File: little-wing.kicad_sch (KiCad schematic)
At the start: 126 parts, among them IC1 AP7335-WG-7, J1 nice!view, J2 Battery, J3 trackball, J4 rotary, J5 trackball, J6 nice!view, J7 Battery, SW1 Power, SW2 Reset, SW3 Reset, SW4 Power, U1 nice!nano v2, U2 PMW3610, U3 nice!nano v2

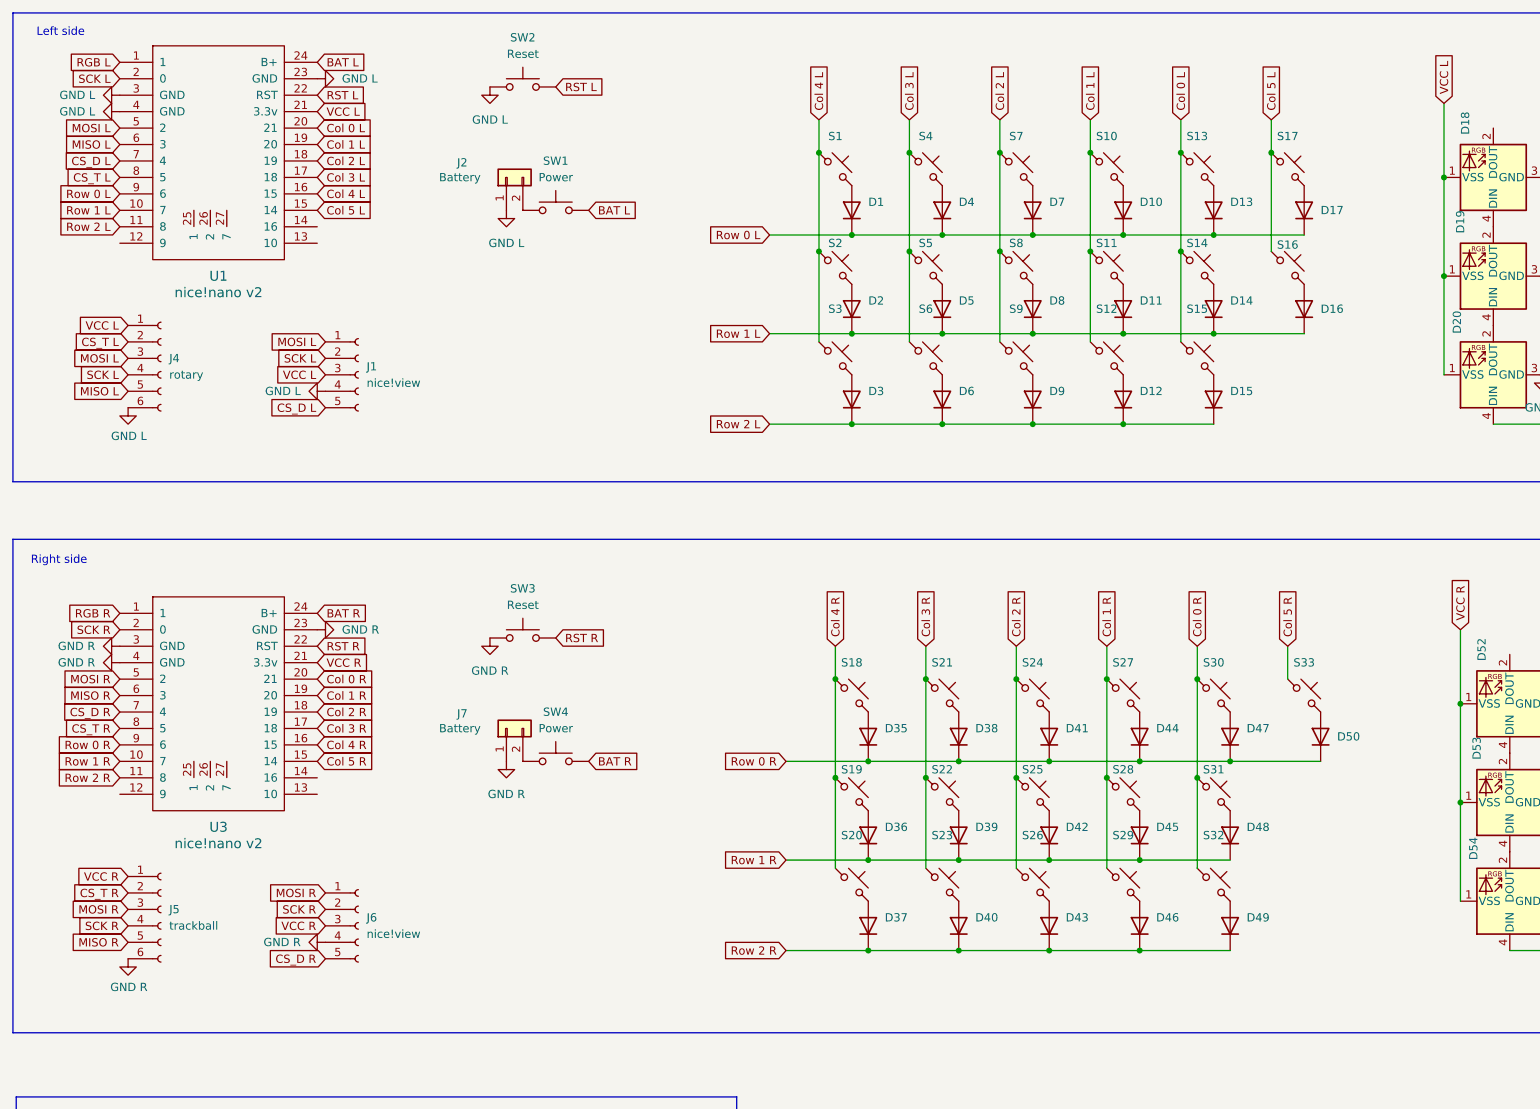
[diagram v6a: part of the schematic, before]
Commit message: Lining up some extra sockets for wiring
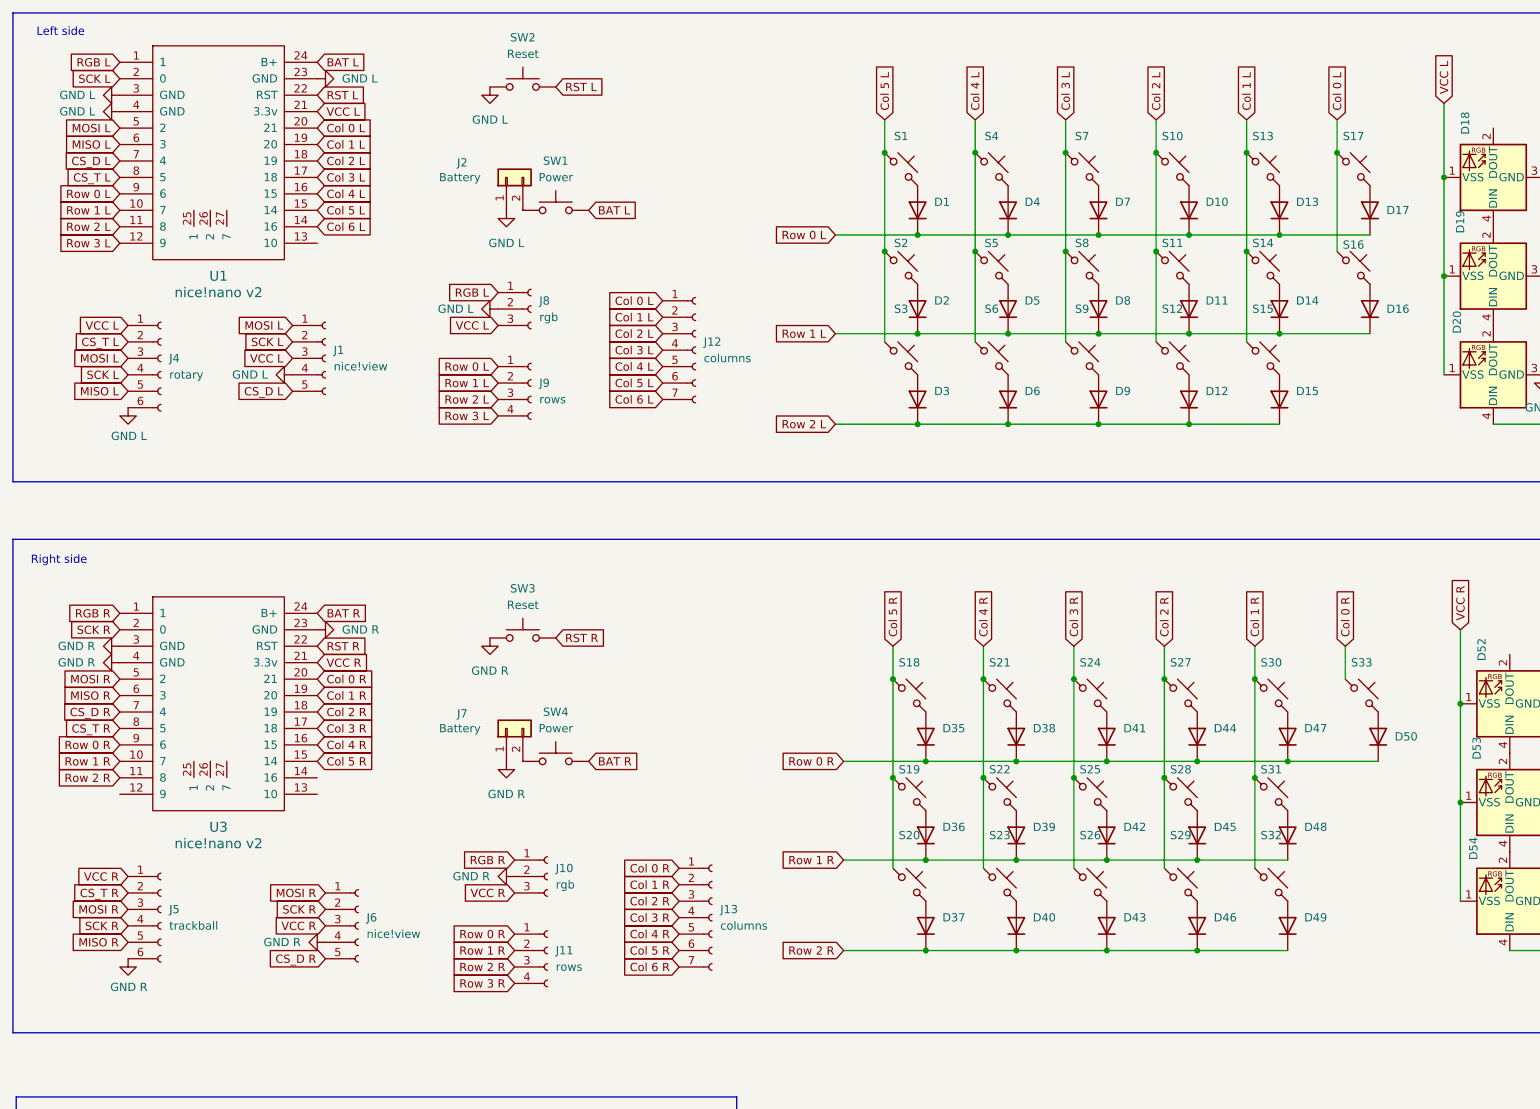
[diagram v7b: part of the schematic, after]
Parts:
- added J10, J8: rgb, Connector_Wuerth:Wuerth_WR-WTB_64800311622_1x03_P1.50mm_Vertical, symbol Connector:Conn_01x03_Socket
- added J11, J9: rows, Connector_Wuerth:Wuerth_WR-WTB_64800411622_1x04_P1.50mm_Vertical, symbol Connector:Conn_01x04_Socket
- added J12, J13: columns, Connector_Wuerth:Wuerth_WR-WTB_64800711622_1x07_P1.50mm_Vertical, symbol Connector:Conn_01x07_Socket
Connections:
- net Col 0 L: now also S16.1, S17.1, J12.1 (Pin_1); no longer S13.1, S14.1, S15.1
- net Col 0 R: now also S33.1, J13.1 (Pin_1); no longer S30.1, S31.1, S32.1
- net Col 1 L: now also S13.1, S14.1, S15.1, J12.2 (Pin_2); no longer S10.1, S11.1, S12.1
- net Col 1 R: now also S30.1, S31.1, S32.1, J13.2 (Pin_2); no longer S27.1, S28.1, S29.1
- net Col 2 L: now also S10.1, S11.1, S12.1, J12.3 (Pin_3); no longer S7.1, S8.1, S9.1
- net Col 2 R: now also S27.1, S28.1, S29.1, J13.3 (Pin_3); no longer S24.1, S25.1, S26.1
- net Col 3 L: now also S7.1, S8.1, S9.1, J12.4 (Pin_4); no longer S4.1, S5.1, S6.1
- net Col 3 R: now also S24.1, S25.1, S26.1, J13.4 (Pin_4); no longer S21.1, S22.1, S23.1
- net Col 4 L: now also S4.1, S5.1, S6.1, J12.5 (Pin_5); no longer S1.1, S2.1, S3.1
- net Col 4 R: now also S21.1, S22.1, S23.1, J13.5 (Pin_5); no longer S18.1, S19.1, S20.1
- net Col 5 L: now also S1.1, S2.1, S3.1, J12.6 (Pin_6); no longer S16.1, S17.1
- net Col 5 R: now also S18.1, S19.1, S20.1, J13.6 (Pin_6); no longer S33.1
- net GND L: now also J8.2 (Pin_2)
- net GND R: now also J10.2 (Pin_2)
- net RGB L: now also J8.1 (Pin_1)
- net RGB R: now also J10.1 (Pin_1)
- net Row 0 L: now also J9.1 (Pin_1)
- net Row 0 R: now also J11.1 (Pin_1)
- net Row 1 L: now also J9.2 (Pin_2)
- net Row 1 R: now also J11.2 (Pin_2)
- net Row 2 L: now also J9.3 (Pin_3)
- net Row 2 R: now also J11.3 (Pin_3)
- net VCC L: now also J8.3 (Pin_3)
- net VCC R: now also J10.3 (Pin_3)
- net Row 3 L: now reaches U1.12 (9)
- net Row 3 L: now also J9.4 (Pin_4)
- net Col 6 L: now reaches U1.14 (16)
- net Col 6 L: now also J12.7 (Pin_7)
- new net Col 6 R: J13.7 (Pin_7)
- new net Row 3 R: J11.4 (Pin_4)
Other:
- moved on the sheet: D1, D10, D11, D12, D13, D14, D15, D16, D17, D2, D3, D35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

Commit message: Wiring together the mobos
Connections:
- net CS_T  L is gone; now on net CS_T L: J4.2 (Pin_2)
- net SCK  L is gone; now on net SCK L: J4.4 (Pin_4)
- net Col 6 R: now also U3.14 (16)
- net Row 3 R: now also U3.12 (9)
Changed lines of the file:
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@@
 		)
 	)
-	(global_label "CS_T  L"
+	(global_label "CS_T L"
 		(shape input)
 		(at 36.83 67.31 180)
@@
 		)
 		(property "Intersheetrefs" "${INTERSHEET_REFS}"
-			(at 26.4668 67.31 0)
+			(at 27.4344 67.31 0)
 			(effects
 				(font
@@
 		)
 	)
-	(global_label "SCK  L"
+	(global_label "SCK L"
 		(shape input)
 		(at 36.83 72.39 180)
@@
 		)
 		(property "Intersheetrefs" "${INTERSHEET_REFS}"
-			(at 27.132 72.39 0)
+			(at 28.0996 72.39 0)
 			(effects
 				(font
@@
 		)
 	)
+	(global_label "Col 6 R"
+		(shape input)
+		(at 66.04 134.62 0)
+		(fields_autoplaced yes)
+		(effects
+			(font
+				(size 1.27 1.27)
+			)
+			(justify left)
+		)
+		(property "Intersheetrefs" "${INTERSHEET_REFS}"
+			(at 76.5241 134.62 0)
+			(effects
+				(font
+					(size 1.27 1.27)
+				)
+				(justify left)
+				(hide yes)
+			)
+		)
+	)
 	(global_label "Row 2 R"
 		(shape input)
@@
 			(effects
 				(font
+					(size 1.27 1.27)
+				)
+				(justify right)
+				(hide yes)
+			)
+		)
+	)
+	(global_label "Row 3 R"
+		(shape input)
+		(at 35.56 137.16 180)
+		(fields_autoplaced yes)
+		(effects
+			(font
+				(size 1.27 1.27)
+			)
+			(justify right)
+		)
+		(property "Intersheetrefs" "${INTERSHEET_REFS}"
+			(at 24.4106 137.16 0)
+			(effects
+				(font
